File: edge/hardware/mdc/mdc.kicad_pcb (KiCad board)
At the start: 2 copper layers, 86.4 x 142.6 mm, 20 parts, among them J1 Conn_01x06, J2 Screw_Terminal_01x02, Q1 2N7000, Q2 2N7000, Q3 2N7000, Q4 2N7000, U1 ESP32-S3-DEVKITC-1-N16R8V, U5 74HC04

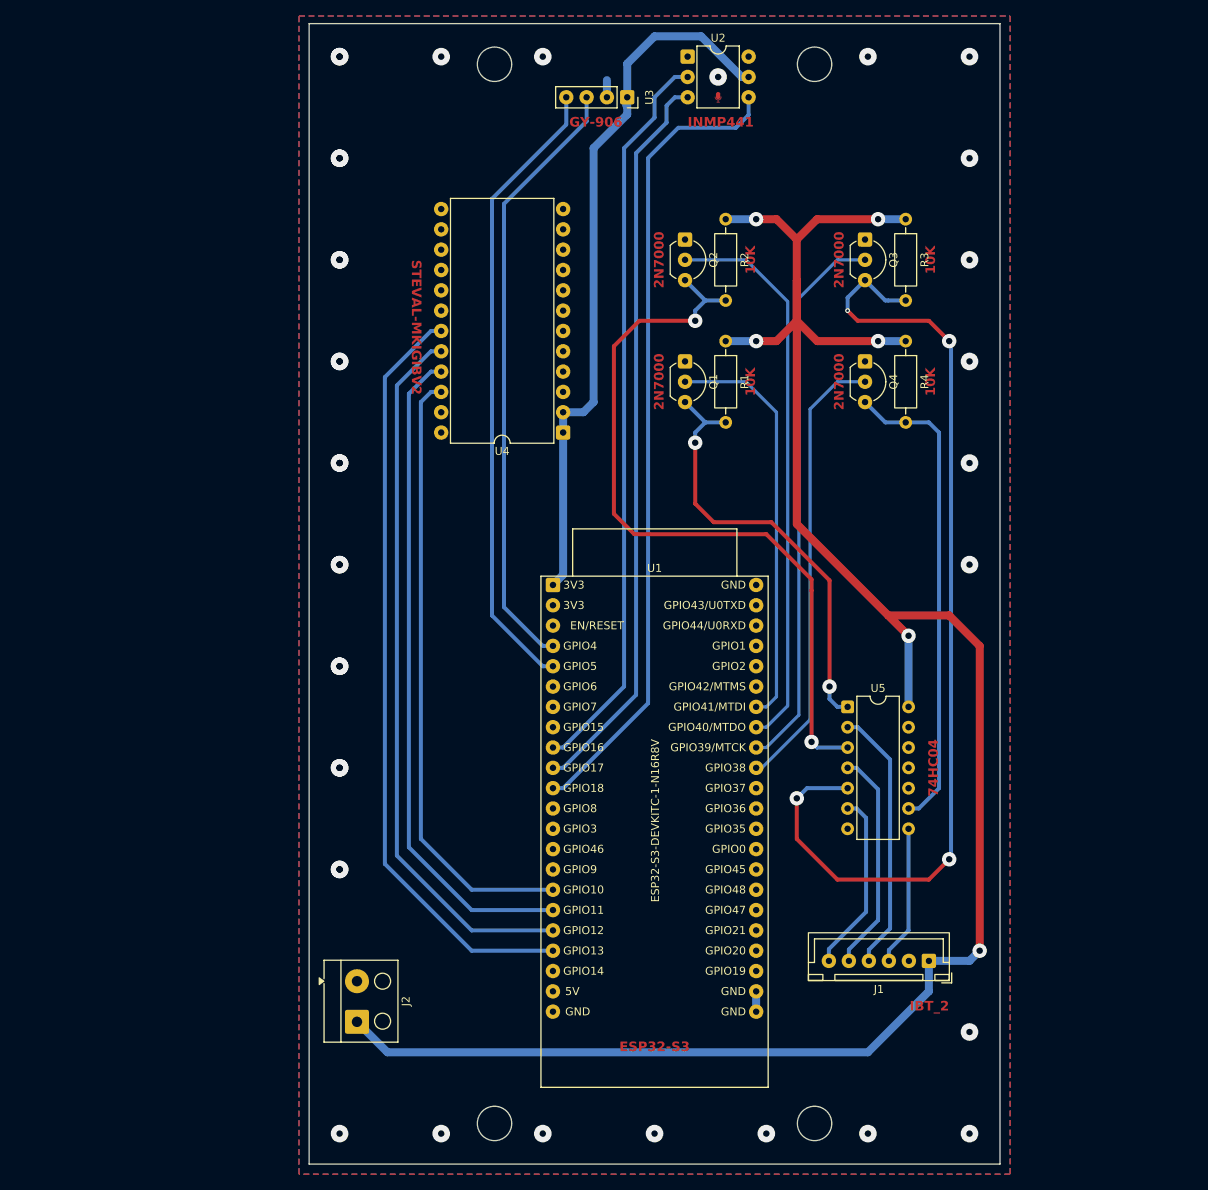
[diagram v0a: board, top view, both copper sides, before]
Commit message: finish rev3.0 PCB layout + data collector script changes + firmware changes
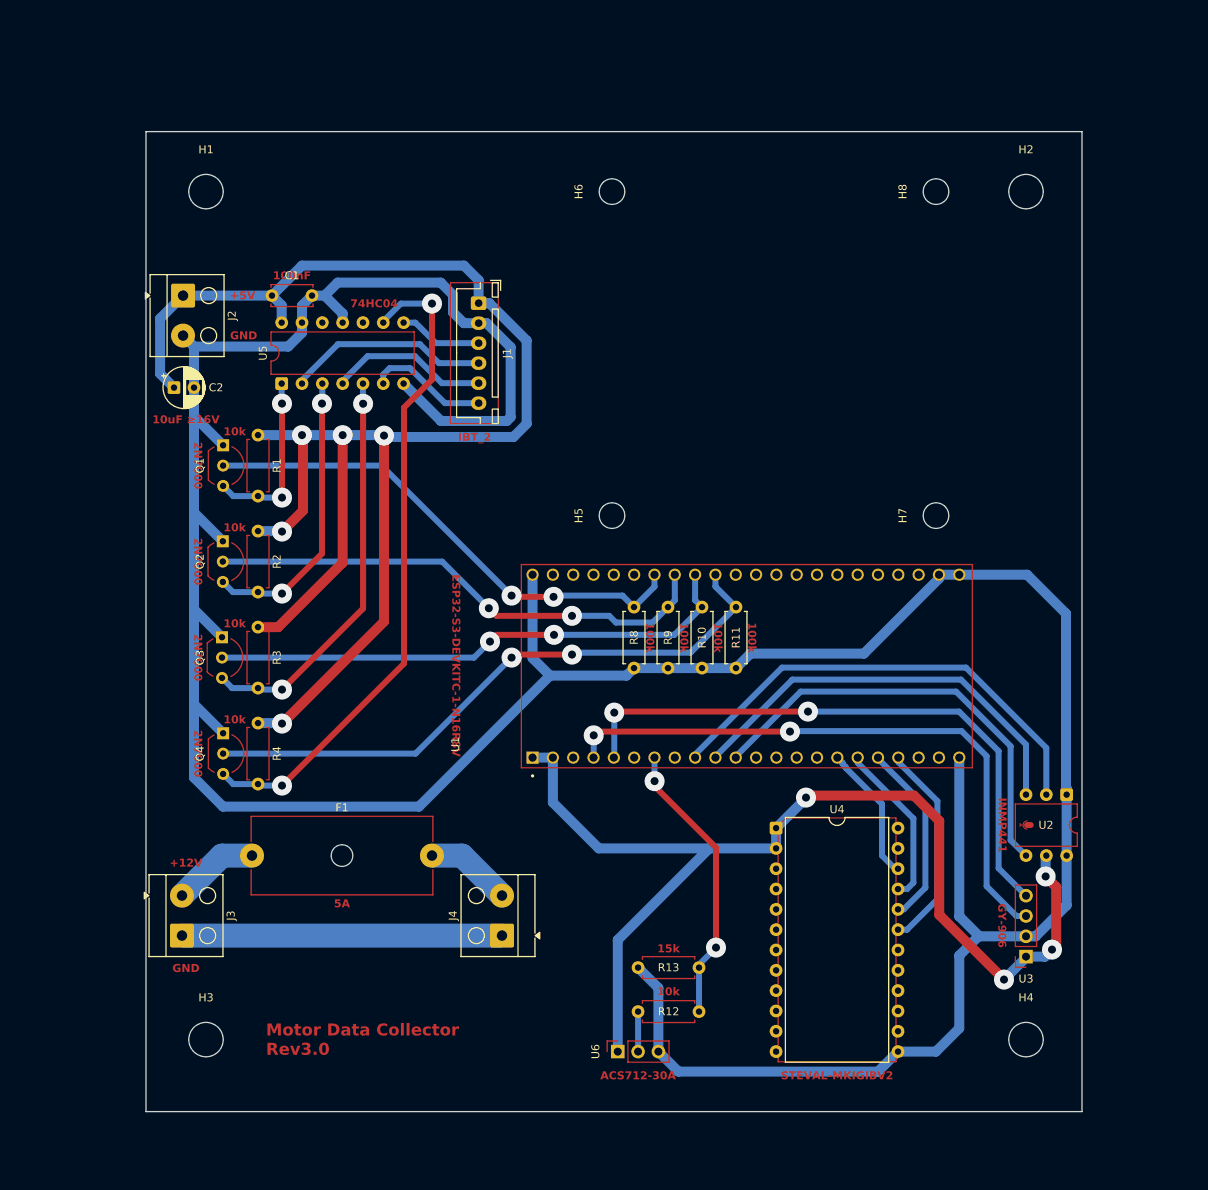
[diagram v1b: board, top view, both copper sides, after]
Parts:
- removed G***: LOGO, LOGO
- added C1: 100nF, Capacitor_THT:C_Disc_D5.0mm_W2.5mm_P5.00mm, F.Cu at (99.5, 54.0)
- added C2: 10uF ≥16V, Capacitor_THT:CP_Radial_D5.0mm_P2.50mm, F.Cu at (87.2, 65.5)
- added F1: 5A, Fuse:Fuseholder_Cylinder-5x20mm_Schurter_0031_8201_Horizontal_Open, F.Cu at (97.0, 124.0)
- added H5: MountingHole, MountingHole:MountingHole_3.2mm_M3, F.Cu at (142.0, 81.5)
- added H6: MountingHole, MountingHole:MountingHole_3.2mm_M3, F.Cu at (142.0, 41.0)
- added H7: MountingHole, MountingHole:MountingHole_3.2mm_M3, F.Cu at (182.5, 81.5)
- added H8: MountingHole, MountingHole:MountingHole_3.2mm_M3, F.Cu at (182.5, 41.0)
- added J3: Screw_Terminal_01x02, TerminalBlock_Altech:Altech_AK100_1x02_P5.00mm, F.Cu at (88.2, 129.0)
- added J4: Screw_Terminal_01x02, TerminalBlock_Altech:Altech_AK100_1x02_P5.00mm, F.Cu at (128.2, 134.0)
- added R10: 100k, Resistor_THT:R_Axial_DIN0207_L6.3mm_D2.5mm_P7.62mm_Horizontal, F.Cu at (153.2, 92.9)
- added R11: 100k, Resistor_THT:R_Axial_DIN0207_L6.3mm_D2.5mm_P7.62mm_Horizontal, F.Cu at (157.5, 92.9)
- added R12: 10k, Resistor_THT:R_Axial_DIN0207_L6.3mm_D2.5mm_P7.62mm_Horizontal, F.Cu at (145.3, 143.5)
- added R13: 15k, Resistor_THT:R_Axial_DIN0207_L6.3mm_D2.5mm_P7.62mm_Horizontal, F.Cu at (152.9, 138.0)
- added R8: 100k, Resistor_THT:R_Axial_DIN0207_L6.3mm_D2.5mm_P7.62mm_Horizontal, F.Cu at (144.8, 92.9)
- added R9: 100k, Resistor_THT:R_Axial_DIN0207_L6.3mm_D2.5mm_P7.62mm_Horizontal, F.Cu at (149.0, 92.9)
- added U6: ACS712-30A, Connector_PinSocket_2.54mm:PinSocket_1x03_P2.54mm_Vertical, F.Cu at (142.7, 148.5)
- J1: value Conn_01x06 -> IBT_2
- R1, R2, R3, R4: value 10K -> 10k; footprint Resistor_THT:R_Axial_DIN0207_L6.3mm_D2.5mm_P10.16mm_Horizontal -> Resistor_THT:R_Axial_DIN0207_L6.3mm_D2.5mm_P7.62mm_Horizontal
- U1: footprint Espressif:ESP32-S3-DevKitC -> ESP32-S3-DEVKITC-1-N16R8V:XCVR_ESP32-S3-DEVKITC-1-N16R8V
- U2: value ~ -> INMP441
- U3: value ~ -> GY-906
- U4: value ~ -> STEVAL-MKIGIBV2
- moved U3 118.4 mm to (193.8, 136.6), turned to 180 degrees
- moved U2 103.7 mm to (198.8, 116.4), turned to -90 degrees
- moved J1 99.6 mm to (125.3, 54.9), turned to -90 degrees
- moved R3 95.7 mm to (97.8, 95.4)
- moved Q3 94.5 mm to (93.2, 96.7)
- moved R4 94.0 mm to (97.8, 107.4)
- moved Q4 92.7 mm to (93.4, 108.7)
- moved J2 88.4 mm to (88.4, 54.0)
- moved U5 81.5 mm to (100.7, 65.0), turned to 90 degrees
- moved R2 70.3 mm to (97.8, 83.4)
- moved Q2 69.0 mm to (93.4, 84.7)
- moved R1 59.6 mm to (97.8, 71.4)
- moved Q1 58.7 mm to (93.4, 72.7)
- moved U4 56.2 mm to (162.5, 120.6), turned to 0 degrees
- moved H1 39.4 mm to (91.2, 41.0)
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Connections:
- U5 pad 10: (no net) -> unconnected-(U5-Pad10)
- U5 pad 11: (no net) -> GND
- U5 pad 12: (no net) -> unconnected-(U5-Pad12)
- U5 pad 13: (no net) -> GND
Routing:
- net GND: track 4.75 -> 430.0 mm, vias 36 -> 0
- net R_EN_IN: track 124.2 -> 50.6 mm, vias 4 -> 2
- net SPI_CS: track 95.8 -> 26.2 mm
- net SPI_SCL: track 89.5 -> 23.3 mm
- net SPI_SDA: track 83.1 -> 20.8 mm
- net SPI_SDO: track 76.8 -> 17.2 mm
- net LPWM_IN: track 94.8 -> 36.3 mm
- net +5V: track 256.5 -> 202.5 mm, vias 6 -> 5
- net +3V3: track 90.2 -> 137.9 mm, vias 0 -> 4
- net I2S_SD: track 101.4 -> 55.2 mm
- net MOTOR_GND: track 0.00 -> 40.0 mm
- net I2S_SCK: track 92.5 -> 52.6 mm
- net ISENSE: track 0.00 -> 35.8 mm, vias 0 -> 2
- net I2S_WS: track 92.5 -> 58.8 mm
- net RPWM_IN: track 55.1 -> 22.2 mm
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- removed copper zone on B.Cu, net GND
- removed copper zone on F.Cu, net GND
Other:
- board size 86.4 x 142.6 mm -> 117 x 122.5 mm
- board text added: "+12V"
- board text added: "+5V"
- board text added: "GND"
- board text added: "IBT_2 Heatsink"
- board text added: "Motor Data Collector Rev3.0"
- board text added: "Terminals"
- board text removed: "10K"
- board text removed: "2N7000"
- board text removed: "74HC04"
- board text removed: "ESP32-S3"
- board text removed: "GY-906"
- board text removed: "IBT_2"
- board text removed: "INMP441"
- board text removed: "STEVAL-MKIGIBV2"

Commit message: update rev3.0 schematic and layout
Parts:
- added C10: 470uF 25V, Capacitor_THT:CP_Radial_D5.0mm_P2.50mm, F.Cu at (197.5, 97.2)
- added C3: 100nF, Capacitor_THT:C_Disc_D5.0mm_W2.5mm_P5.00mm, F.Cu at (178.8, 36.0)
- added C4: 100nF, Capacitor_THT:C_Disc_D5.0mm_W2.5mm_P5.00mm, F.Cu at (173.2, 97.5)
- added C5: 10uF 16V, Capacitor_THT:CP_Radial_D5.0mm_P2.50mm, F.Cu at (168.2, 93.8)
- added C6: 100nF, Capacitor_THT:C_Disc_D5.0mm_W2.5mm_P5.00mm, F.Cu at (160.0, 77.8)
- added C7: 100nF, Capacitor_THT:C_Disc_D5.0mm_W2.5mm_P5.00mm, F.Cu at (202.2, 84.0)
- added C8: 100nF, Capacitor_THT:C_Disc_D5.0mm_W2.5mm_P5.00mm, F.Cu at (187.8, 39.0)
- added C9: 100nF, Capacitor_THT:C_Disc_D5.0mm_W2.5mm_P5.00mm, F.Cu at (189.3, 56.6)
- added D1: 10V 1W, Diode_THT:D_DO-41_SOD81_P7.62mm_Horizontal, F.Cu at (196.4, 116.8)
- added Q5: IRF4905, Package_TO_SOT_THT:TO-220-3_Vertical, F.Cu at (191.6, 122.2)
- added Q6: NDP6020P, Package_TO_SOT_THT:TO-220-3_Vertical, F.Cu at (75.8, 119.4)
- added R14: 100k, Resistor_THT:R_Axial_DIN0207_L6.3mm_D2.5mm_P7.62mm_Horizontal, F.Cu at (188.8, 111.2)
- added R15: 100k, Resistor_THT:R_Axial_DIN0207_L6.3mm_D2.5mm_P7.62mm_Horizontal, F.Cu at (82.0, 118.2)
- C2: value 10uF ≥16V -> 10uF 16V
- F1: value 5A -> 6A
- J1: value IBT_2 -> Conn_01x06
- R1, R2, R3, R4: value 10k -> 2.2k
- moved H2 118.2 mm to (75.8, 33.0), turned to 90 degrees
- moved H4 114.5 mm to (204.3, 33.0), turned to 90 degrees
- moved H3 113.6 mm to (204.3, 135.4), turned to 90 degrees
- moved H8 106.7 mm to (75.8, 44.2), turned to 180 degrees
- moved U3 103.7 mm to (193.9, 33.0), turned to -90 degrees
- moved J3 98.5 mm to (186.3, 138.2), turned to 0 degrees
- moved H1 95.7 mm to (75.8, 135.4), turned to 90 degrees
- moved U2 92.4 mm to (172.4, 27.9), turned to 0 degrees
- moved U6 90.2 mm to (205.8, 84.0), turned to 180 degrees
- moved F1 84.5 mm to (181.3, 129.7), turned to 90 degrees
- moved J2 84.3 mm to (86.2, 138.2), turned to 0 degrees
- moved H6 79.3 mm to (75.8, 84.7), turned to 180 degrees
- moved R12 77.7 mm to (196.8, 85.3), turned to 90 degrees
- moved H7 76.0 mm to (116.3, 44.2), turned to 180 degrees
- moved Q4 73.2 mm to (161.9, 134.6), turned to 0 degrees
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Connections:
- F1 pad 1: +12V -> Net-(Q5-D)
- J2 pad 1: +5V -> Net-(J2-Pin_1)
- U5 pad 10: unconnected-(U5-Pad10) -> GND
- U5 pad 11: GND -> unconnected-(U5-Pad11)
- U5 pad 12: unconnected-(U5-Pad12) -> GND
- U5 pad 13: GND -> unconnected-(U5-Pad13)
- U6 pad 1: +3V3 -> +5V
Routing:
- net GND: track 430.0 -> 596.2 mm, vias 0 -> 2
- net +5V: track 202.5 -> 347.2 mm, vias 5 -> 8
- net GPIO41: track 63.9 -> 93.8 mm, vias 2 -> 0
- net L_EN_IN: track 83.2 -> 104.9 mm
- net GPIO40: track 64.0 -> 83.8 mm, vias 2 -> 0
- net +3V3: track 137.9 -> 156.6 mm, vias 4 -> 5
- net Net-(J2-Pin_1): track 0.00 -> 18.1 mm
- net +12V: track 10.8 -> 27.1 mm
- net +12V_FUSED: track 10.8 -> 24.0 mm
- net MOTOR_GND: track 40.0 -> 53.1 mm
- net I2S_SD: track 55.2 -> 42.8 mm, vias 0 -> 2
- net I2C_SDA: track 75.3 -> 62.9 mm
- net Net-(Q5-D): track 0.00 -> 12.3 mm
- net Net-(D1-A): track 0.00 -> 12.1 mm
- net GPIO39: track 67.0 -> 77.0 mm, vias 2 -> 0
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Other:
- board size 117 x 122.5 mm -> 145 x 117 mm
- board text added: "10uF 16V"
- board text added: "470uF 25V"
- board text added: "IBT_2"
- board text added: "Rev3.0 Motor Data Collector"
- board text removed: "Motor Data Collector Rev3.0"

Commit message: update rev3.0 schematic and layout
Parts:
- removed D1: 10V 1W, Diode_THT:D_DO-41_SOD81_P7.62mm_Horizontal
- removed Q6: NDP6020P, Package_TO_SOT_THT:TO-220-3_Vertical
- C10: footprint Capacitor_THT:CP_Radial_D5.0mm_P2.50mm -> Capacitor_THT:CP_Radial_D8.0mm_P3.50mm
- J2, J3, J4: value Screw_Terminal_01x02 -> Conn_01x02; footprint TerminalBlock_Altech:Altech_AK100_1x02_P5.00mm -> Connector_JST:JST_VH_B2P-VH-B_1x02_P3.96mm_Vertical
- Q5: value IRF4905 -> IRFZ44N
- R15: value 100k -> 10k
- moved R15 107.6 mm to (189.5, 116.8), turned to 90 degrees
- moved R14 8.14 mm to (194.8, 116.8), turned to 90 degrees
- moved J4 4.76 mm to (186.5, 98.4), turned to 0 degrees
- moved J2 4.51 mm to (90.8, 138.5), turned to 180 degrees
- moved J3 4.21 mm to (190.5, 138.5), turned to 180 degrees
- moved C10 1.78 mm to (199.2, 96.8)
- moved Q5 0.55 mm to (191.0, 122.2)
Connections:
- F1 pad 1: Net-(Q5-D) -> +12V
- J2 pad 1: Net-(J2-Pin_1) -> GND
- J2 pad 2: GND -> +5V
- J3 pad 1: MOTOR_GND -> Net-(J3-Pin_1)
- J4 pad 1: MOTOR_GND -> +12V_FUSED
- J4 pad 2: +12V_FUSED -> MOTOR_GND
- Q5 pad 1: Net-(D1-A) -> Net-(Q5-G)
- Q5 pad 2: Net-(Q5-D) -> Net-(J3-Pin_1)
- Q5 pad 3: +12V -> MOTOR_GND
- R14 pad 1: Net-(D1-A) -> Net-(Q5-G)
- R15 pad 1: Net-(Q6-G) -> Net-(Q5-G)
- R15 pad 2: GND -> +12V
- U5 pad 10: GND -> unconnected-(U5-Pad10)
- U5 pad 11: unconnected-(U5-Pad11) -> GND
- U5 pad 12: GND -> unconnected-(U5-Pad12)
- U5 pad 13: unconnected-(U5-Pad13) -> GND
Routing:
- net GND: track 596.2 -> 576.4 mm
- net Net-(J3-Pin_1): track 0.00 -> 18.9 mm
- net Net-(J2-Pin_1): track 18.1 -> 0.00 mm
- net Net-(Q5-D): track 12.3 -> 0.00 mm
- net Net-(D1-A): track 12.1 -> 0.00 mm
- net Net-(Q5-G): track 0.00 -> 9.24 mm
- net +12V: track 27.1 -> 34.9 mm
- net MOTOR_GND: track 53.1 -> 45.3 mm
- net Net-(Q6-G): track 6.71 -> 0.00 mm
- net +5V: track 347.2 -> 343.9 mm
- net +12V_FUSED: track 24.0 -> 26.8 mm

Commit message: added rev3.1 + some ML adjustments
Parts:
- removed Q5: IRFZ44N, Package_TO_SOT_THT:TO-220-3_Vertical
- removed R14: 100k, Resistor_THT:R_Axial_DIN0207_L6.3mm_D2.5mm_P7.62mm_Horizontal
- removed R15: 10k, Resistor_THT:R_Axial_DIN0207_L6.3mm_D2.5mm_P7.62mm_Horizontal
- F1: value 6A -> T10A
- J2, J3, J4: footprint Connector_JST:JST_VH_B2P-VH-B_1x02_P3.96mm_Vertical -> TerminalBlock:TerminalBlock_MaiXu_MX126-5.0-02P_1x02_P5.00mm
- moved F1 5.20 mm to (186.5, 129.7)
- moved R10 3.91 mm to (132.5, 69.4)
- moved R11 3.91 mm to (132.5, 65.2)
- moved R8 3.91 mm to (132.5, 77.9)
- moved R9 3.91 mm to (132.5, 73.7)
- moved U1 1.11 mm to (150.9, 60.8)
- moved J3 0.99 mm to (191.5, 138.5)
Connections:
- J3 pad 1: Net-(J3-Pin_1) -> MOTOR_GND
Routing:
- net GND: track 576.4 -> 30.4 mm, vias 2 -> 5
- net +12V: track 34.9 -> 8.80 mm
- net Net-(J3-Pin_1): track 18.9 -> 0.00 mm
- net Net-(Q5-G): track 9.24 -> 0.00 mm
- net GPIO41: track 93.8 -> 97.7 mm
- net GPIO40: track 83.8 -> 87.7 mm
- net GPIO39: track 77.0 -> 80.9 mm
- net MOTOR_GND: track 45.3 -> 48.6 mm
- net GPIO38: track 83.4 -> 86.7 mm
- net +12V_FUSED: track 26.8 -> 24.7 mm
- net +5V: track 343.9 -> 343.3 mm
- added copper zone on B.Cu, net GND
- added copper zone on F.Cu, net GND
